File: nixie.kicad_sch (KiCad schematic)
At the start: 15 parts, among them Q1 IRF840A, U1 UC3843_DIP8

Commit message: update
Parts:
- added R10: 0.5, symbol Device:R
- added R11: 1, symbol Device:R
- added R7: 15k, symbol Device:R
- added R8: 1M, symbol Device:R
- added R9: 0.7, symbol Device:R
- R1: value 2.2k -> 20k
- R3: value 20k -> 22
- R5: value 2.2k -> 47k
- R6: value 10k -> 15k
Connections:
- net 0: now also R7.1
- net VC1: now also R11.2; no longer D1.1 (K), R5.2
- net VCC: now also R10.2; no longer L1.1
- net at R2.1, U1.1 (COMP): now also R8.1
- net at Q1.3 (S), R4.1, U1.3 (CS): now also R5.2; no longer R5.1
- net at L1.2, Q1.2 (D): now also R9.1; no longer D1.2 (A)
- net at Q1.1 (G), R3.2: now also R5.1
- new net: L1.1, R10.1
- new net: D1.1 (K), R11.1
- new net: D1.2 (A), R9.2
- new net: R7.2, R8.2
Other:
- note added: "nixie tube load"
- moved on the sheet: C4, D1

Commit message: working w/ simulation
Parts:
- R2: value 15K -> 22k
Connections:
- net VC1: now also R7.2, R8.2
- net at R2.1, U1.1 (COMP): no longer R8.1
- net at C3.2, R6.2, U1.2 (FB): now also R8.1
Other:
- note added: ".options method=gear .options reltol=0.01 .options abstol=1e-6 .options vntol-1e-4"
- note added: "R9, R10, R11 are NOT supposed to be in the real fabrication they are just so the simulation runs"
- moved on the sheet: R8

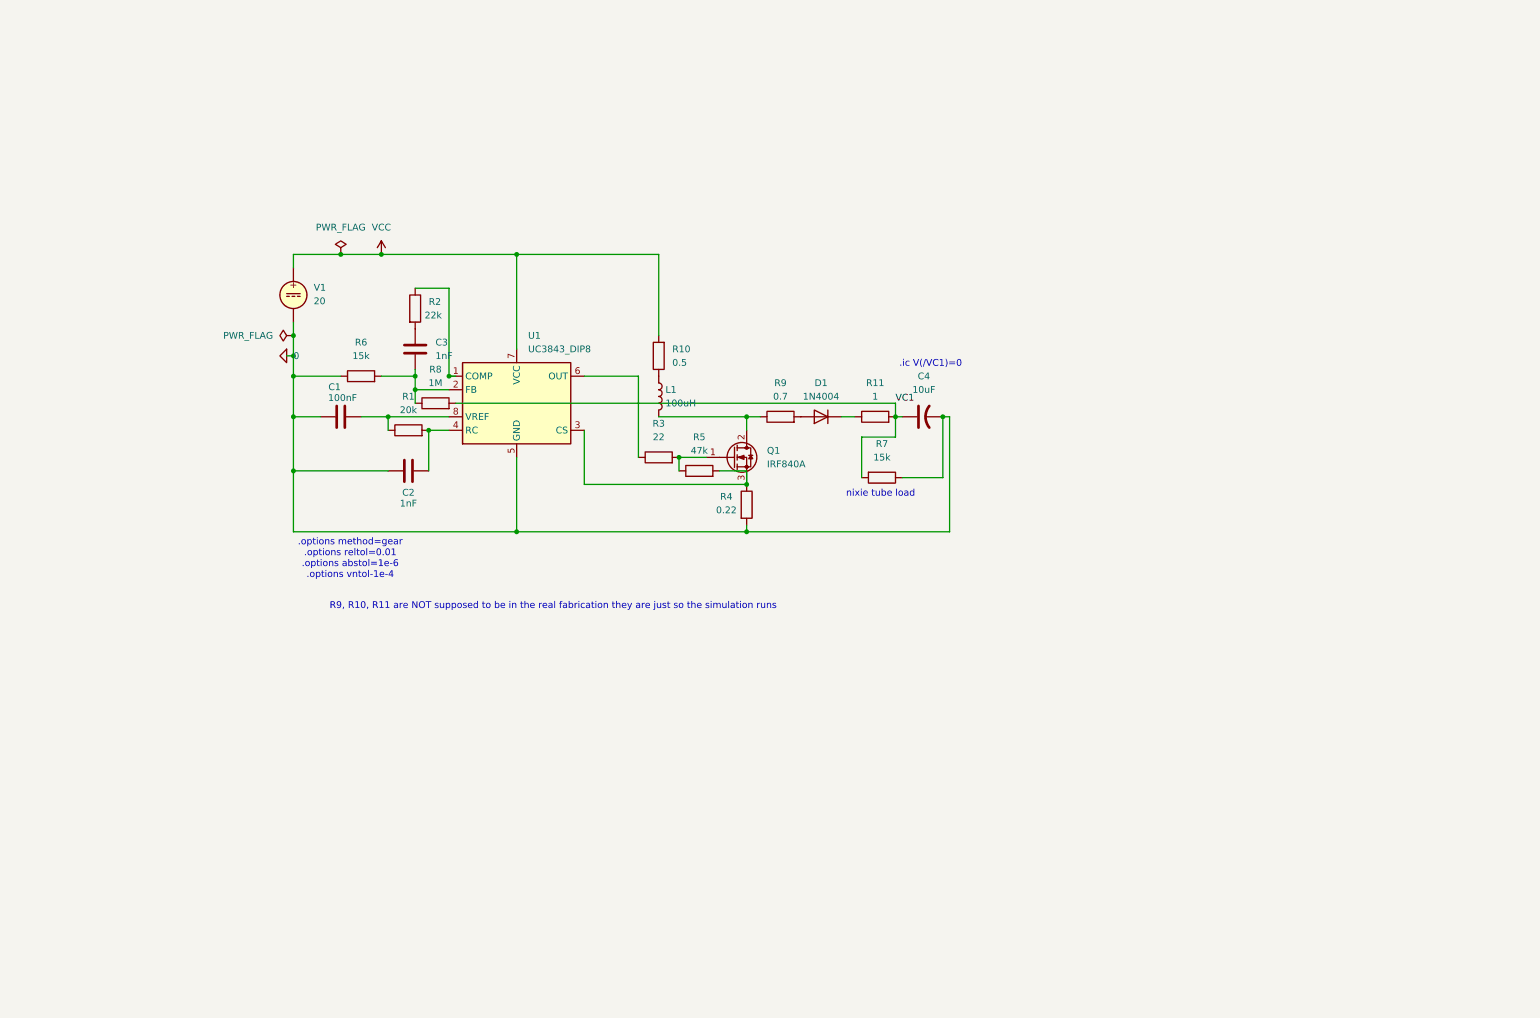
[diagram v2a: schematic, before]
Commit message: added nixie parts and esp32. did not wire hv5622 yet bc i didn't know how to do so cleanly without overlapping wire.
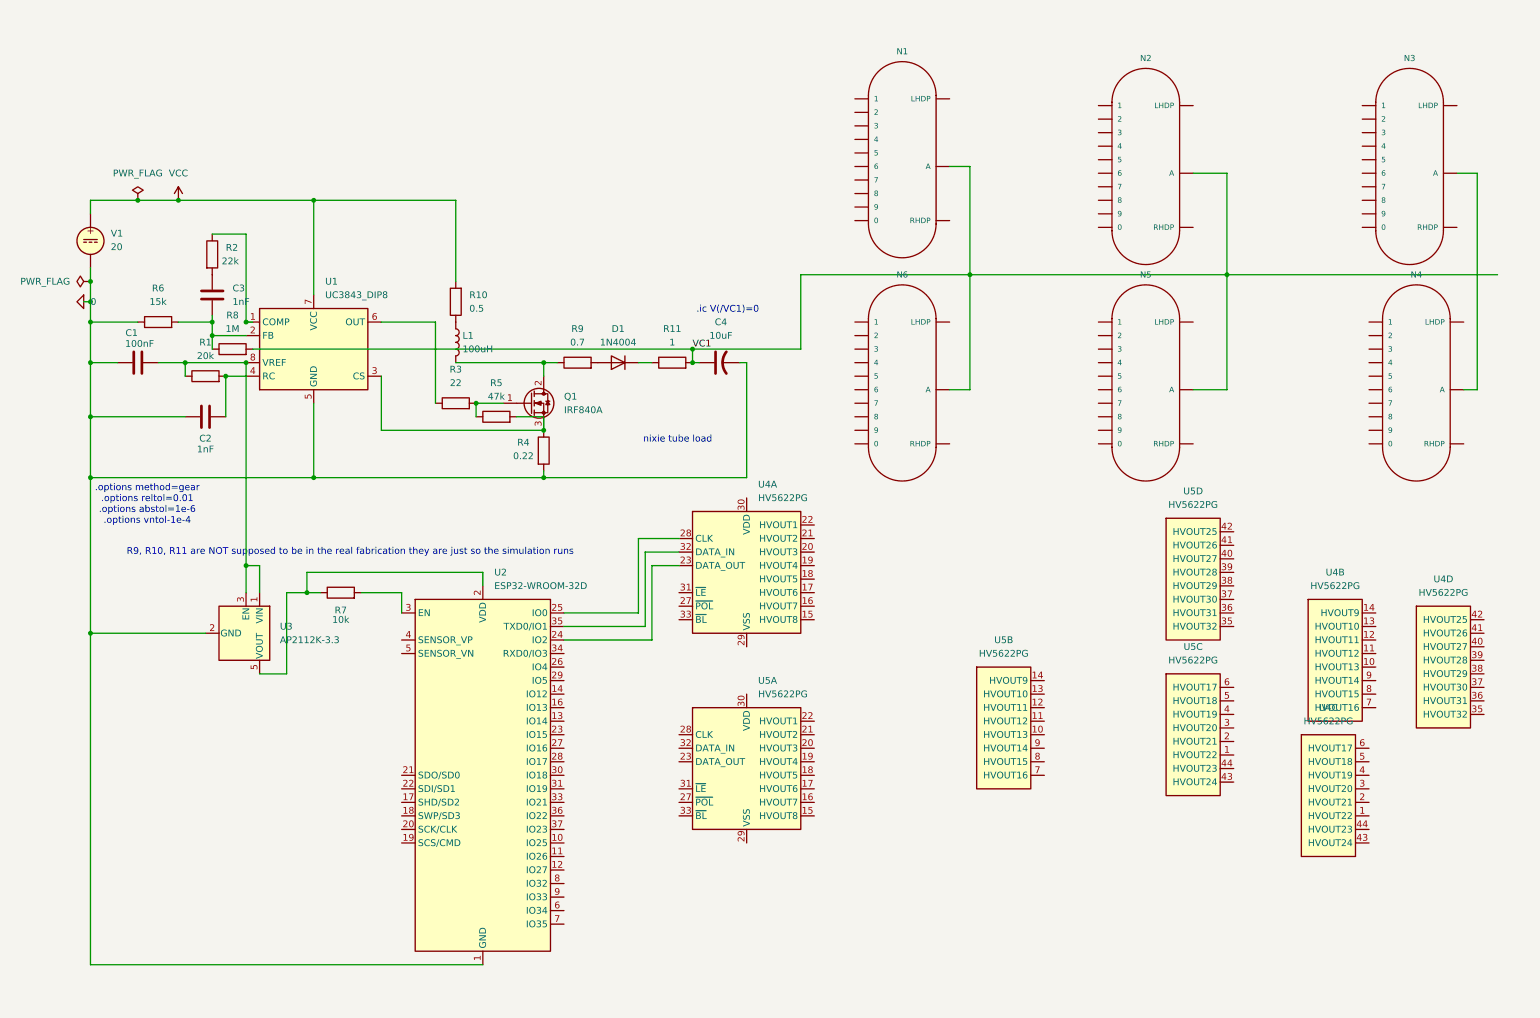
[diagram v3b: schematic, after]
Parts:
- added N1, N2, N3, N4, N5, N6: IN-14, nixies-us_IN-14, symbol nixies-us:IN-14
- added U2: ESP32-WROOM-32D, RF_Module:ESP32-WROOM-32D, symbol RF_Module:ESP32-WROOM-32D
- added U3: AP2112K-3.3, Package_TO_SOT_SMD:SOT-23-5, symbol Regulator_Linear:AP2112K-3.3
- added U4, U5: HV5622PG, Package_QFP:PQFP-44_10x10mm_P0.8mm, symbol Driver_Display:HV5622PG
- R7: value 15k -> 10k
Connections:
- net 0: now also U2.1 (GND), U2.15 (GND), U2.38 (GND), U2.39 (GND), U3.2 (GND); no longer R7.1
- net VC1: now also N1.A, N2.A, N5.A, N6.A; no longer R7.2
- net at C1.2, R1.1, U1.8 (VREF): now also U3.1 (VIN), U3.3 (EN)
- new net: U2.24 (IO2), U4.23 (DATA_OUT)
- new net: U2.25 (IO0), U4.28 (CLK)
- new net: U2.35 (TXD0/IO1), U4.32 (DATA_IN)
- new net: N3.A, N4.A
- new net: R7.1, U2.2 (VDD), U3.5 (VOUT)
- new net: R7.2, U2.3 (EN)
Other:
- moved on the sheet: C1, C2, C3, C4, D1, L1, Q1, R1, R10, R11, R2, R3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

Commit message: new stuff
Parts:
- C1, C2, C3, C4: footprint (none) -> Capacitor_SMD:C_0402_1005Metric
- L1: footprint (none) -> Inductor_SMD:L_7.3x7.3_H4.5
- N1, N2, N3, N4, N5, N6: footprint nixies-us_IN-14 -> nixies-us:nixies-us-IN-14
- R1, R10, R11, R2, R3, R4, R5, R6, R7, R8, R9: footprint (none) -> Resistor_SMD:R_0402_1005Metric
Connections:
- net 0: now also U4.29 (VSS), U5.29 (VSS)
- net VC1: now also N3.A, N4.A
- net at C1.2, R1.1, U1.8 (VREF)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: now also U4.30 (VDD), U5.30 (VDD)
- net A8: now reaches U4.15 (HVOUT8)
- net A8: now also N1.8
- net A7: now reaches U4.16 (HVOUT7)
- net A7: now also N1.7
- net A6: now reaches U4.17 (HVOUT6)
- net A6: now also N1.6
- net A5: now reaches U4.18 (HVOUT5)
- net A5: now also N1.5
- net A4: now reaches U4.19 (HVOUT4)
- net A4: now also N1.4
- net A3: now reaches U4.20 (HVOUT3)
- net A3: now also N1.3
- net A2: now reaches U4.21 (HVOUT2)
- net A2: now also N1.2
- net A1: now reaches U4.22 (HVOUT1)
- net A1: now also N1.1
- net D8: now reaches U5.15 (HVOUT8)
- net D8: now also N6.8
- net D7: now reaches U5.16 (HVOUT7)
- net D7: now also N6.7
- net D6: now reaches U5.17 (HVOUT6)
- net D6: now also N6.6
- net D5: now reaches U5.18 (HVOUT5)
- net D5: now also N6.5
- net D4: now reaches U5.19 (HVOUT4)
- net D4: now also N6.4
- net D3: now reaches U5.20 (HVOUT3)
- net D3: now also N6.3
- net D2: now reaches U5.21 (HVOUT2)
- net D2: now also N6.2
- net D1: now reaches U5.22 (HVOUT1)
- net D1: now also N6.1
- net at U5.23 (DATA_OUT): now also U2.29 (IO5)
- net at U5.28 (CLK): now also U2.34 (RXD0/IO3)
- net at U5.32 (DATA_IN): now also U2.26 (IO4)
- net F2: now reaches U5.1 (HVOUT22)
- net F2: now also N4.2
- net F1: now reaches U5.2 (HVOUT21)
- net F1: now also N4.1
- net E10: now reaches U5.3 (HVOUT20)
- net E10: now also N5.0
- net E9: now reaches U5.4 (HVOUT19)
- net E9: now also N5.9
- net F4: now reaches U5.43 (HVOUT24)
- net F4: now also N4.4
- net F3: now reaches U5.44 (HVOUT23)
- net F3: now also N4.3
- net E8: now reaches U5.5 (HVOUT18)
- net E8: now also N5.8
- net E7: now reaches U5.6 (HVOUT17)
- net E7: now also N5.7
- net C10: now reaches N3.0
- net C10: now also U4.37 (HVOUT30)
- net C1: now reaches N3.1
- net C1: now also U4.2 (HVOUT21)
- net C2: now reaches N3.2
- net C2: now also U4.1 (HVOUT22)
- net C3: now reaches N3.3
- net C3: now also U4.44 (HVOUT23)
- net C4: now reaches N3.4
- net C4: now also U4.43 (HVOUT24)
- net C5: now reaches N3.5
- net C5: now also U4.42 (HVOUT25)
- net C6: now reaches N3.6
- net C6: now also U4.41 (HVOUT26)
- net C7: now reaches N3.7
- net C7: now also U4.40 (HVOUT27)
- net C8: now reaches N3.8
- net C8: now also U4.39 (HVOUT28)
- net C9: now reaches N3.9
- net C9: now also U4.38 (HVOUT29)
- net B10: now reaches N2.0
- net B10: now also U4.3 (HVOUT20)
- net B1: now reaches N2.1
- net B1: now also U4.12 (HVOUT11)
- net B2: now reaches N2.2
- net B2: now also U4.11 (HVOUT12)
- net B3: now reaches N2.3
- net B3: now also U4.10 (HVOUT13)
- net B4: now reaches N2.4
- net B4: now also U4.9 (HVOUT14)
- net B5: now reaches N2.5
- net B5: now also U4.8 (HVOUT15)
- net B6: now reaches N2.6
- net B6: now also U4.7 (HVOUT16)
- net B7: now reaches N2.7
- net B7: now also U4.6 (HVOUT17)
- net B8: now reaches N2.8
- net B8: now also U4.5 (HVOUT18)
- net B9: now reaches N2.9
- net B9: now also U4.4 (HVOUT19)
- net F10: now reaches U5.37 (HVOUT30)
- net F10: now also N4.0
- net F9: now reaches U5.38 (HVOUT29)
- net F9: now also N4.9
- net F8: now reaches U5.39 (HVOUT28)
- net F8: now also N4.8
- net F7: now reaches U5.40 (HVOUT27)
- net F7: now also N4.7
- net F6: now reaches U5.41 (HVOUT26)
- net F6: now also N4.6
- net F5: now reaches U5.42 (HVOUT25)
- net F5: now also N4.5
- net E1: now reaches N5.1
- net E1: now also U5.12 (HVOUT11)
- net E2: now reaches N5.2
- net E2: now also U5.11 (HVOUT12)
- net E3: now reaches N5.3
- net E3: now also U5.10 (HVOUT13)
- net E4: now reaches N5.4
- net E4: now also U5.9 (HVOUT14)
- net E5: now reaches N5.5
- net E5: now also U5.8 (HVOUT15)
- net E6: now reaches N5.6
- net E6: now also U5.7 (HVOUT16)
- net D10: now reaches U5.13 (HVOUT10)
- net D10: now also N6.0
- net D9: now reaches U5.14 (HVOUT9)
- net D9: now also N6.9
- net A10: now reaches N1.0
- net A10: now also U4.13 (HVOUT10)
- net A9: now reaches N1.9
- net A9: now also U4.14 (HVOUT9)
- no-connect marks 0 -> 48
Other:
- moved on the sheet: N1, N6, U4B, U4C, U4D, U5B, U5C, U5D

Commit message: fix pr
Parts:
- removed R10: 0.5, Resistor_SMD:R_0402_1005Metric, symbol Device:R
- removed R11: 1, Resistor_SMD:R_0402_1005Metric, symbol Device:R
- removed R9: 0.7, Resistor_SMD:R_0402_1005Metric, symbol Device:R
- removed U2: ESP32-WROOM-32D, RF_Module:ESP32-WROOM-32D, symbol RF_Module:ESP32-WROOM-32D
- added SW1: DOWNLOAD, Button_Switch_SMD:SW_Push_1P1T_NO_CK_KSC6xxJ, symbol Switch:SW_Push
- added U6: ESP32-S3-MINI-1, RF_Module:ESP32-S2-MINI-1, symbol RF_Module:ESP32-S3-MINI-1
- C4: footprint Capacitor_SMD:C_0402_1005Metric -> Capacitor_SMD:CP_Elec_10x12.5
- L1: footprint Inductor_SMD:L_7.3x7.3_H4.5 -> Inductor_SMD:L_TaiTech_TMPC1265_13.5x12.5mm
- R1, R2, R3, R5, R6, R7, R8: footprint Resistor_SMD:R_0402_1005Metric -> Resistor_SMD:R_1210_3225Metric
- R4: footprint Resistor_SMD:R_0402_1005Metric -> Resistor_SMD:R_2512_6332Metric
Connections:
- net 0: now also SW1.1, U6.1 (GND), U6.2 (GND), U6.42 (GND), U6.43 (GND), U6.46 (GND), U6.47 (GND), U6.48 (GND), U6.49 (GND), U6.50 (GND), U6.51 (GND), U6.52 (GND), U6.53 (GND), U6.54 (GND), U6.55 (GND), U6.56 (GND), U6.57 (GND), U6.58 (GND), U6.59 (GND), U6.60 (GND), U6.61 (GND), U6.62 (GND), U6.63 (GND), U6.64 (GND), U6.65 (GND); no longer U4.29 (VSS), U5.29 (VSS)
- net VC1: now also C3.2, D1.1 (K), R6.2, R8.1, U1.2 (FB)
- net VCC: now also L1.1
- net at C1.2, R1.1, U1.8 (VREF)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: no longer U4.30 (VDD), U5.30 (VDD)
- net at L1.2, Q1.2 (D): now also D1.2 (A)
- net at U4.23 (DATA_OUT): now also U6.28 (IO33)
- net at U4.28 (CLK): now also U6.25 (IO21)
- net at U4.32 (DATA_IN): now also U6.26 (IO26)
- net at U5.23 (DATA_OUT): now also U6.32 (IO36)
- net at U5.28 (CLK): now also U6.29 (IO34)
- net at U5.32 (DATA_IN): now also U6.31 (IO35)
- net at R7.1, U3.5 (VOUT): now also U6.3 (3V3)
- net at R7.2: now also SW1.2, U6.4 (IO0), U6.44 (IO46), U6.45 (EN)
- net at U5.35 (HVOUT32): now also N1.2
- net at U5.36 (HVOUT31): now also N1.1
- net A1: no longer names the net of U4.22 (HVOUT1)
- net A1: now also N6.1; no longer N1.1
- net A10: no longer names the net of N1.0
- net A10: now also U5.15 (HVOUT8); no longer U4.13 (HVOUT10)
- net A2: no longer names the net of U4.21 (HVOUT2)
- net A2: now also N6.2; no longer N1.2
- net A3: no longer names the net of U4.20 (HVOUT3)
- net A3: now also N6.3; no longer N1.3
- net A4: no longer names the net of U4.19 (HVOUT4)
- net A4: now also N6.4; no longer N1.4
- net A5: no longer names the net of U4.18 (HVOUT5)
- net A5: now also N6.5; no longer N1.5
- net A6: no longer names the net of U4.17 (HVOUT6)
- net A6: now also N6.6; no longer N1.6
- net A7: no longer names the net of U4.16 (HVOUT7)
- net A7: now also N6.7; no longer N1.7
- net A8: no longer names the net of U4.15 (HVOUT8)
- net A8: now also N6.8; no longer N1.8
- net A9: no longer names the net of N1.9
- net A9: now also U5.16 (HVOUT7); no longer U4.14 (HVOUT9)
- net B1: no longer names the net of N2.1
- net B1: now also U5.2 (HVOUT21); no longer U4.12 (HVOUT11)
- net B10: no longer names the net of N2.0
- net B10: now also U5.37 (HVOUT30); no longer U4.3 (HVOUT20)
- net B2: no longer names the net of N2.2
- net B2: now also U5.1 (HVOUT22); no longer U4.11 (HVOUT12)
- net B3: no longer names the net of N2.3
- net B3: now also U5.44 (HVOUT23); no longer U4.10 (HVOUT13)
- net B4: no longer names the net of N2.4
- net B4: now also U5.43 (HVOUT24); no longer U4.9 (HVOUT14)
- net B5: no longer names the net of N2.5
- net B5: now also U5.42 (HVOUT25); no longer U4.8 (HVOUT15)
- net B6: no longer names the net of N2.6
- net B6: now also U5.41 (HVOUT26); no longer U4.7 (HVOUT16)
- net B7: no longer names the net of N2.7
- net B7: now also U5.40 (HVOUT27); no longer U4.6 (HVOUT17)
- net B8: no longer names the net of N2.8
- net B8: now also U5.39 (HVOUT28); no longer U4.5 (HVOUT18)
- net B9: no longer names the net of N2.9
- net B9: now also U5.38 (HVOUT29); no longer U4.4 (HVOUT19)
- net C1: no longer names the net of N3.1
- net C1: now also U5.12 (HVOUT11); no longer U4.2 (HVOUT21)
- net C10: no longer names the net of N3.0
- net C10: now also U5.3 (HVOUT20); no longer U4.37 (HVOUT30)
- net C2: no longer names the net of N3.2
- net C2: now also U5.11 (HVOUT12); no longer U4.1 (HVOUT22)
- net C3: no longer names the net of N3.3
- net C3: now also U5.10 (HVOUT13); no longer U4.44 (HVOUT23)
- net C4: no longer names the net of N3.4
- net C4: now also U5.9 (HVOUT14); no longer U4.43 (HVOUT24)
- net C5: no longer names the net of N3.5
- net C5: now also U5.8 (HVOUT15); no longer U4.42 (HVOUT25)
- net C6: no longer names the net of N3.6
- net C6: now also U5.7 (HVOUT16); no longer U4.41 (HVOUT26)
- net C7: no longer names the net of N3.7
- net C7: now also U5.6 (HVOUT17); no longer U4.40 (HVOUT27)
- net C8: no longer names the net of N3.8
- net C8: now also U5.5 (HVOUT18); no longer U4.39 (HVOUT28)
- net C9: no longer names the net of N3.9
- net C9: now also U5.4 (HVOUT19); no longer U4.38 (HVOUT29)
- net D1: no longer names the net of U5.22 (HVOUT1)
- net D1: now also N1.3; no longer N6.1
- net D10: no longer names the net of U5.13 (HVOUT10)
- net D10: no longer N6.0
- net D2: no longer names the net of U5.21 (HVOUT2)
- net D2: now also N1.4; no longer N6.2
- net D3: no longer names the net of U5.20 (HVOUT3)
- net D3: now also N1.5; no longer N6.3
- net D4: no longer names the net of U5.19 (HVOUT4)
- net D4: now also N1.6; no longer N6.4
- net D5: no longer names the net of U5.18 (HVOUT5)
- net D5: now also N1.7; no longer N6.5
- net D6: no longer names the net of U5.17 (HVOUT6)
- net D6: now also N1.8; no longer N6.6
- removed net D7: N6.7, U5.16 (HVOUT7)
- removed net D8: N6.8, U5.15 (HVOUT8)
- net D9: no longer names the net of U5.14 (HVOUT9)
- net D9: no longer N6.9
- net E1: no longer names the net of N5.1
- net E1: now also U4.12 (HVOUT11); no longer U5.12 (HVOUT11)
- net E10: no longer names the net of N5.0
- net E10: now also U4.3 (HVOUT20); no longer U5.3 (HVOUT20)
- net E2: no longer names the net of N5.2
- net E2: now also U4.11 (HVOUT12); no longer U5.11 (HVOUT12)
- net E3: no longer names the net of N5.3
- net E3: now also U4.10 (HVOUT13); no longer U5.10 (HVOUT13)
- net E4: no longer names the net of N5.4
- net E4: now also U4.9 (HVOUT14); no longer U5.9 (HVOUT14)
- net E5: no longer names the net of N5.5
- net E5: now also U4.8 (HVOUT15); no longer U5.8 (HVOUT15)
- net E6: no longer names the net of N5.6
- net E6: now also U4.7 (HVOUT16); no longer U5.7 (HVOUT16)
- net E7: no longer names the net of N5.7
- net E7: now also U4.6 (HVOUT17); no longer U5.6 (HVOUT17)
- net E8: no longer names the net of N5.8
- net E8: now also U4.5 (HVOUT18); no longer U5.5 (HVOUT18)
- net E9: no longer names the net of N5.9
- net E9: now also U4.4 (HVOUT19); no longer U5.4 (HVOUT19)
- net F1: no longer names the net of N4.1
- net F1: now also U4.2 (HVOUT21); no longer U5.2 (HVOUT21)
- net F10: no longer names the net of N4.0
- net F10: now also U4.37 (HVOUT30); no longer U5.37 (HVOUT30)
- net F2: no longer names the net of N4.2
- net F2: now also U4.1 (HVOUT22); no longer U5.1 (HVOUT22)
- net F3: no longer names the net of N4.3
- net F3: now also U4.44 (HVOUT23); no longer U5.44 (HVOUT23)
- net F4: no longer names the net of N4.4
- net F4: now also U4.43 (HVOUT24); no longer U5.43 (HVOUT24)
- net F5: no longer names the net of N4.5
- net F5: now also U4.42 (HVOUT25); no longer U5.42 (HVOUT25)
- net F6: no longer names the net of N4.6
- net F6: now also U4.41 (HVOUT26); no longer U5.41 (HVOUT26)
- net F7: no longer names the net of N4.7
- net F7: now also U4.40 (HVOUT27); no longer U5.40 (HVOUT27)
- net F8: no longer names the net of N4.8
- net F8: now also U4.39 (HVOUT28); no longer U5.39 (HVOUT28)
- net F9: no longer names the net of N4.9
- net F9: now also U4.38 (HVOUT29); no longer U5.38 (HVOUT29)
- new net: N6.0, U4.13 (HVOUT10)
- new net: N6.9, U4.14 (HVOUT9)
- no-connect marks 48 -> 0
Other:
- note removed: "nixie tube load"
- company: (none) -> Alex Matysik and Christian Janev
- title: (none) -> Nixie Tube Controller
- moved on the sheet: N1, N2, N3, N4, N5, N6, U4B, U4C, U4D, U5A, U5B, U5C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
